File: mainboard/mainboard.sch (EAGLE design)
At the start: 1 part, among them IC1 ATMEGA168-PU

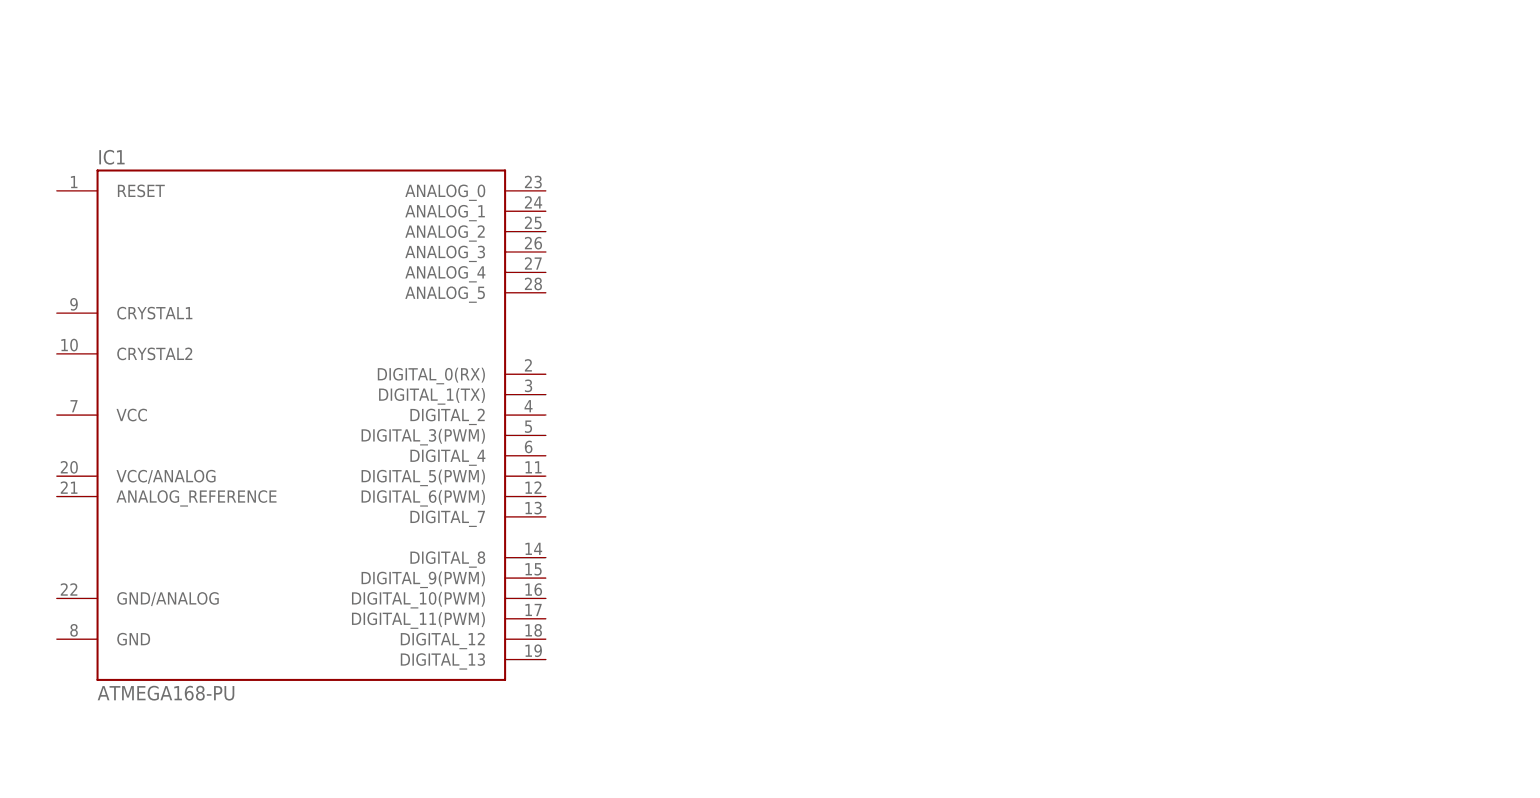
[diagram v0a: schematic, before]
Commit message: complete arduino usb with usb & programming header
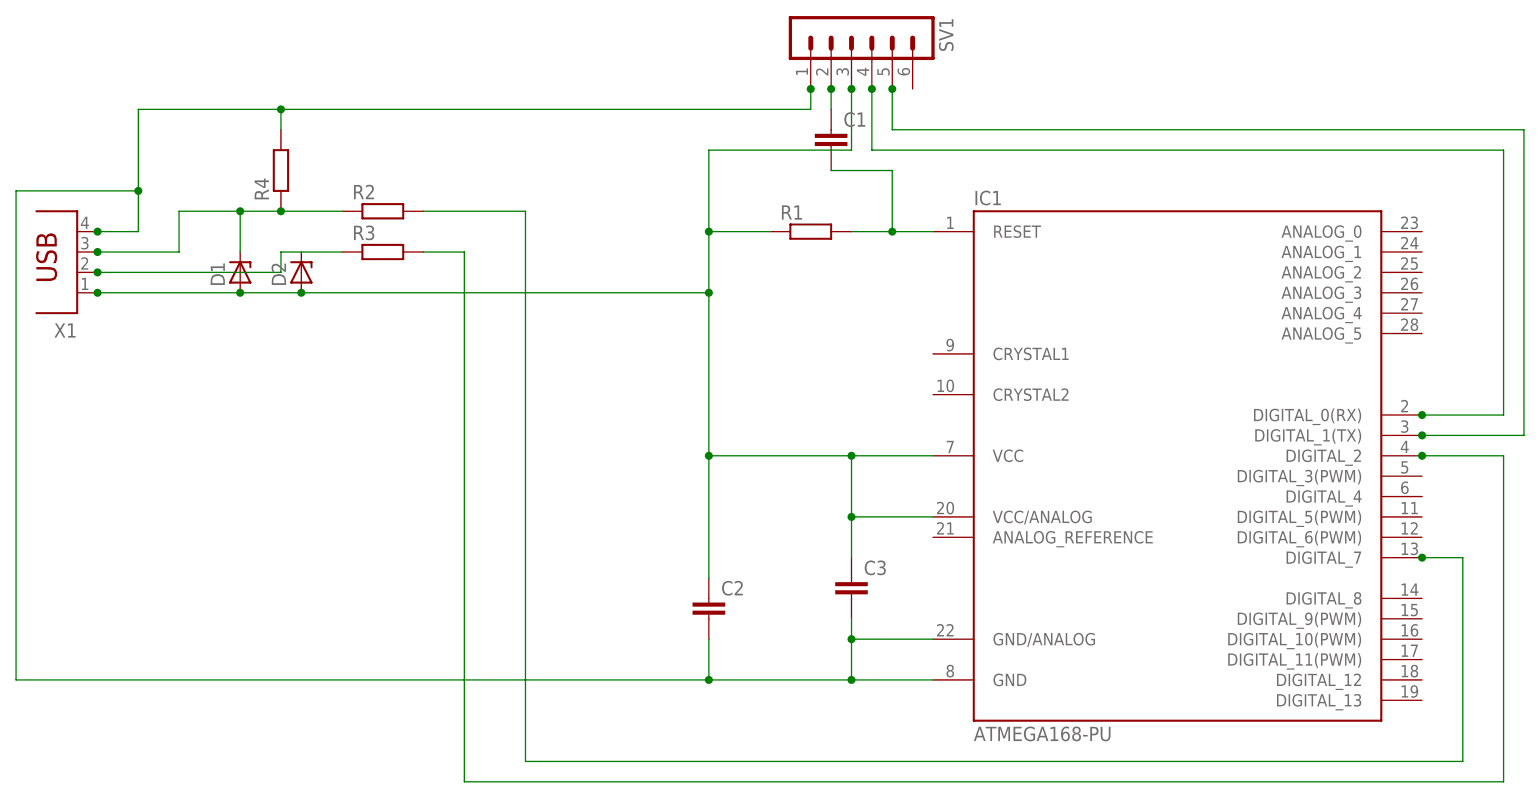
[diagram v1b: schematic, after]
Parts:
- added C1, C2, C3: (no value), capacitor-wima:C2,5-3
- added D1, D2: (no value), diode:ZENER-DIODEZD-5
- added R1, R2, R3, R4: (no value), resistor:R-EU_0204/7
- added SV1: (no value), con-lstb:MA06-1
- added X1: (no value), con-berg:PN61729
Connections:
- new net N$1: C1.2, IC1.RESET, R1.2
- new net N$10: IC1.DIGITAL_2, R3.2
- new net N$11: IC1.DIGITAL_7, R2.2
- new net N$2: D1.C, R2.1, R4.1, X1.3
- new net N$4: C1.1, SV1.2
- new net N$5: R3.1, X1.2
- new net N$6: IC1.DIGITAL_0(RX), SV1.4
- new net N$7: IC1.DIGITAL_1(TX), SV1.5
- new net N$8: C2.2, C3.2, IC1.GND, IC1.GND/ANALOG, R4.2, SV1.1, X1.4
- new net N$9: C2.1, C3.1, D1.A, D2.A, IC1.VCC, IC1.VCC/ANALOG, R1.1, SV1.3, X1.1
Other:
- moved on the sheet: IC1
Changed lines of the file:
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@@
 <parts>
 <part name="IC1" library="Arduino-AVR" deviceset="ATMEGA168-PU" device=""/>
+<part name="R1" library="resistor" deviceset="R-EU_" device="0204/7"/>
+<part name="C2" library="capacitor-wima" deviceset="C" device="2,5-3"/>
+<part name="C3" library="capacitor-wima" deviceset="C" device="2,5-3"/>
+<part name="SV1" library="con-lstb" deviceset="MA06-1" device=""/>
+<part name="C1" library="capacitor-wima" deviceset="C" device="2,5-3"/>
+<part name="X1" library="con-berg" deviceset="PN61729" device=""/>
+<part name="R2" library="resistor" deviceset="R-EU_" device="0204/7"/>
+<part name="R3" library="resistor" deviceset="R-EU_" device="0204/7"/>
+<part name="R4" library="resistor" deviceset="R-EU_" device="0204/7"/>
+<part name="D1" library="diode" deviceset="ZENER-DIODE" device="ZD-5"/>
+<part name="D2" library="diode" deviceset="ZENER-DIODE" device="ZD-5"/>
 </parts>
 <sheets>
@@
 </plain>
 <instances>
-<instance part="IC1" gate="1" x="-17.78" y="30.48"/>
+<instance part="IC1" gate="1" x="91.44" y="25.4"/>
+<instance part="R1" gate="G$1" x="45.72" y="53.34"/>
+<instance part="C2" gate="G$1" x="33.02" y="7.62"/>
+<instance part="C3" gate="G$1" x="50.8" y="10.16"/>
+<instance part="SV1" gate="1" x="53.34" y="78.74" rot="R270"/>
+<instance part="C1" gate="G$1" x="48.26" y="66.04"/>
+<instance part="X1" gate="G$1" x="-45.72" y="50.8" rot="R180"/>
+<instance part="R2" gate="G$1" x="-7.62" y="55.88"/>
+<instance part="R3" gate="G$1" x="-7.62" y="50.8"/>
+<instance part="R4" gate="G$1" x="-20.32" y="60.96" rot="R90"/>
+<instance part="D1" gate="G$1" x="-25.4" y="48.26" rot="R90"/>
+<instance part="D2" gate="G$1" x="-17.78" y="48.26" rot="R90"/>
 </instances>
 <busses>
 </busses>
 <nets>
+<net name="N$1" class="0">
+<segment>
+<pinref part="IC1" gate="1" pin="RESET"/>
+<pinref part="R1" gate="G$1" pin="2"/>
+<wire x1="50.8" y1="53.34" x2="55.88" y2="53.34" width="0.1524" layer="91"/>
+<pinref part="C1" gate="G$1" pin="2"/>
+<wire x1="55.88" y1="53.34" x2="60.96" y2="53.34" width="0.1524" layer="91"/>
+<wire x1="48.26" y1="60.96" x2="55.88" y2="60.96" width="0.1524" layer="91"/>
+<wire x1="55.88" y1="60.96" x2="55.88" y2="53.34" width="0.1524" layer="91"/>
+<junction x="55.88" y="53.34"/>
+</segment>
+</net>
+<net name="N$4" class="0">
+<segment>
+<pinref part="SV1" gate="1" pin="2"/>
+<pinref part="C1" gate="G$1" pin="1"/>
+<wire x1="48.26" y1="71.12" x2="48.26" y2="68.58" width="0.1524" layer="91"/>
+<junction x="48.26" y="71.12"/>
+</segment>
+</net>
+<net name="N$6" class="0">
+<segment>
+<pinref part="SV1" gate="1" pin="4"/>
+<wire x1="53.34" y1="71.12" x2="53.34" y2="63.5" width="0.1524" layer="91"/>
+<wire x1="53.34" y1="63.5" x2="132.08" y2="63.5" width="0.1524" layer="91"/>
+<wire x1="132.08" y1="63.5" x2="132.08" y2="30.48" width="0.1524" layer="91"/>
+<pinref part="IC1" gate="1" pin="DIGITAL_0(RX)"/>
+<wire x1="132.08" y1="30.48" x2="121.92" y2="30.48" width="0.1524" layer="91"/>
+<junction x="121.92" y="30.48"/>
+<junction x="53.34" y="71.12"/>
+</segment>
+</net>
+<net name="N$7" class="0">
+<segment>
+<pinref part="SV1" gate="1" pin="5"/>
+<wire x1="55.88" y1="71.12" x2="55.88" y2="66.04" width="0.1524" layer="91"/>
+<wire x1="55.88" y1="66.04" x2="134.62" y2="66.04" width="0.1524" layer="91"/>
+<wire x1="134.62" y1="66.04" x2="134.62" y2="27.94" width="0.1524" layer="91"/>
+<pinref part="IC1" gate="1" pin="DIGITAL_1(TX)"/>
+<wire x1="134.62" y1="27.94" x2="121.92" y2="27.94" width="0.1524" layer="91"/>
+<junction x="121.92" y="27.94"/>
+<junction x="55.88" y="71.12"/>
+</segment>
+</net>
+<net name="N$8" class="0">
+<segment>
+<pinref part="SV1" gate="1" pin="1"/>
+<junction x="45.72" y="71.12"/>
+<wire x1="45.72" y1="68.58" x2="45.72" y2="71.12" width="0.1524" layer="91"/>
+<wire x1="-38.1" y1="68.58" x2="-20.32" y2="68.58" width="0.1524" layer="91"/>
+<pinref part="IC1" gate="1" pin="GND"/>
+<pinref part="C2" gate="G$1" pin="2"/>
+<wire x1="-20.32" y1="68.58" x2="45.72" y2="68.58" width="0.1524" layer="91"/>
+<wire x1="60.96" y1="-2.54" x2="50.8" y2="-2.54" width="0.1524" layer="91"/>
+<wire x1="50.8" y1="-2.54" x2="33.02" y2="-2.54" width="0.1524" layer="91"/>
+<wire x1="33.02" y1="-2.54" x2="33.02" y2="2.54" width="0.1524" layer="91"/>
+<junction x="50.8" y="-2.54"/>
+<junction x="33.02" y="-2.54"/>
+<pinref part="IC1" gate="1" pin="GND/ANALOG"/>
+<wire x1="60.96" y1="2.54" x2="50.8" y2="2.54" width="0.1524" layer="91"/>
+<pinref part="C3" gate="G$1" pin="2"/>
+<wire x1="50.8" y1="2.54" x2="50.8" y2="5.08" width="0.1524" layer="91"/>
+<wire x1="50.8" y1="-2.54" x2="50.8" y2="2.54" width="0.1524" layer="91"/>
+<junction x="50.8" y="2.54"/>
+<wire x1="33.02" y1="-2.54" x2="-53.34" y2="-2.54" width="0.1524" layer="91"/>
+<wire x1="-53.34" y1="-2.54" x2="-53.34" y2="58.42" width="0.1524" layer="91"/>
+<wire x1="-53.34" y1="58.42" x2="-38.1" y2="58.42" width="0.1524" layer="91"/>
+<wire x1="-38.1" y1="58.42" x2="-38.1" y2="53.34" width="0.1524" layer="91"/>
+<pinref part="X1" gate="G$1" pin="4"/>
+<wire x1="-38.1" y1="53.34" x2="-43.18" y2="53.34" width="0.1524" layer="91"/>
+<wire x1="-38.1" y1="68.58" x2="-38.1" y2="58.42" width="0.1524" layer="91"/>
+<pinref part="R4" gate="G$1" pin="2"/>
+<wire x1="-20.32" y1="66.04" x2="-20.32" y2="68.58" width="0.1524" layer="91"/>
+<junction x="-20.32" y="68.58"/>
+<junction x="-43.18" y="53.34"/>
+<junction x="-38.1" y="58.42"/>
+</segment>
+</net>
+<net name="N$9" class="0">
+<segment>
+<pinref part="SV1" gate="1" pin="3"/>
+<junction x="50.8" y="71.12"/>
+<wire x1="50.8" y1="63.5" x2="50.8" y2="71.12" width="0.1524" layer="91"/>
+<wire x1="50.8" y1="63.5" x2="33.02" y2="63.5" width="0.1524" layer="91"/>
+<pinref part="IC1" gate="1" pin="VCC/ANALOG"/>
+<wire x1="60.96" y1="17.78" x2="50.8" y2="17.78" width="0.1524" layer="91"/>
+<pinref part="C3" gate="G$1" pin="1"/>
+<wire x1="50.8" y1="17.78" x2="50.8" y2="12.7" width="0.1524" layer="91"/>
+<pinref part="C2" gate="G$1" pin="1"/>
+<wire x1="33.02" y1="10.16" x2="33.02" y2="25.4" width="0.1524" layer="91"/>
+<wire x1="33.02" y1="25.4" x2="33.02" y2="45.72" width="0.1524" layer="91"/>
+<pinref part="R1" gate="G$1" pin="1"/>
+<wire x1="33.02" y1="45.72" x2="33.02" y2="53.34" width="0.1524" layer="91"/>
+<wire x1="40.64" y1="53.34" x2="33.02" y2="53.34" width="0.1524" layer="91"/>
+<pinref part="IC1" gate="1" pin="VCC"/>
+<wire x1="60.96" y1="25.4" x2="50.8" y2="25.4" width="0.1524" layer="91"/>
+<junction x="33.02" y="25.4"/>
+<wire x1="50.8" y1="25.4" x2="33.02" y2="25.4" width="0.1524" layer="91"/>
+<wire x1="50.8" y1="17.78" x2="50.8" y2="25.4" width="0.1524" layer="91"/>
+<junction x="50.8" y="25.4"/>
+<junction x="50.8" y="17.78"/>
+<wire x1="33.02" y1="63.5" x2="33.02" y2="53.34" width="0.1524" layer="91"/>
+<pinref part="X1" gate="G$1" pin="1"/>
+<wire x1="-43.18" y1="45.72" x2="-25.4" y2="45.72" width="0.1524" layer="91"/>
+<pinref part="D1" gate="G$1" pin="A"/>
+<wire x1="-25.4" y1="45.72" x2="-17.78" y2="45.72" width="0.1524" layer="91"/>
+<junction x="-25.4" y="45.72"/>
+<pinref part="D2" gate="G$1" pin="A"/>
+<wire x1="-17.78" y1="45.72" x2="33.02" y2="45.72" width="0.1524" layer="91"/>
+<junction x="-17.78" y="45.72"/>
+<junction x="-43.18" y="45.72"/>
+<junction x="33.02" y="45.72"/>
+<junction x="33.02" y="53.34"/>
+</segment>
+</net>
+<net name="N$2" class="0">
+<segment>
+<pinref part="X1" gate="G$1" pin="3"/>
+<wire x1="-43.18" y1="50.8" x2="-33.02" y2="50.8" width="0.1524" layer="91"/>
+<wire x1="-33.02" y1="50.8" x2="-33.02" y2="55.88" width="0.1524" layer="91"/>
+<pinref part="R2" gate="G$1" pin="1"/>
+<wire x1="-33.02" y1="55.88" x2="-25.4" y2="55.88" width="0.1524" layer="91"/>
+<pinref part="D1" gate="G$1" pin="C"/>
+<wire x1="-25.4" y1="55.88" x2="-20.32" y2="55.88" width="0.1524" layer="91"/>
+<wire x1="-20.32" y1="55.88" x2="-12.7" y2="55.88" width="0.1524" layer="91"/>
+<wire x1="-25.4" y1="50.8" x2="-25.4" y2="55.88" width="0.1524" layer="91"/>
+<pinref part="R4" gate="G$1" pin="1"/>
+<junction x="-20.32" y="55.88"/>
+<junction x="-25.4" y="55.88"/>
+<junction x="-43.18" y="50.8"/>
+</segment>
+</net>
+<net name="N$5" class="0">
+<segment>
+<pinref part="X1" gate="G$1" pin="2"/>
+<wire x1="-43.18" y1="48.26" x2="-20.32" y2="48.26" width="0.1524" layer="91"/>
+<wire x1="-20.32" y1="48.26" x2="-20.32" y2="50.8" width="0.1524" layer="91"/>
+<pinref part="R3" gate="G$1" pin="1"/>
+<wire x1="-20.32" y1="50.8" x2="-12.7" y2="50.8" width="0.1524" layer="91"/>
+<junction x="-43.18" y="48.26"/>
+</segment>
+</net>
+<net name="N$10" class="0">
+<segment>
+<pinref part="R3" gate="G$1" pin="2"/>
+<wire x1="-2.54" y1="50.8" x2="2.54" y2="50.8" width="0.1524" layer="91"/>
+<wire x1="2.54" y1="50.8" x2="2.54" y2="-15.24" width="0.1524" layer="91"/>
+<wire x1="2.54" y1="-15.24" x2="132.08" y2="-15.24" width="0.1524" layer="91"/>
+<wire x1="132.08" y1="-15.24" x2="132.08" y2="25.4" width="0.1524" layer="91"/>
+<pinref part="IC1" gate="1" pin="DIGITAL_2"/>
+<wire x1="132.08" y1="25.4" x2="121.92" y2="25.4" width="0.1524" layer="91"/>
+<junction x="121.92" y="25.4"/>
+</segment>
+</net>
+<net name="N$11" class="0">
+<segment>
+<pinref part="R2" gate="G$1" pin="2"/>
+<wire x1="-2.54" y1="55.88" x2="10.16" y2="55.88" width="0.1524" layer="91"/>
+<wire x1="10.16" y1="55.88" x2="10.16" y2="-12.7" width="0.1524" layer="91"/>
+<wire x1="10.16" y1="-12.7" x2="127" y2="-12.7" width="0.1524" layer="91"/>
+<wire x1="127" y1="-12.7" x2="127" y2="12.7" width="0.1524" layer="91"/>
+<pinref part="IC1" gate="1" pin="DIGITAL_7"/>
+<wire x1="127" y1="12.7" x2="121.92" y2="12.7" width="0.1524" layer="91"/>
+<junction x="121.92" y="12.7"/>
+</segment>
+</net>
 </nets>
 </sheet>
 </sheets>
+<errors>
+</errors>
 </schematic>
 </drawing>

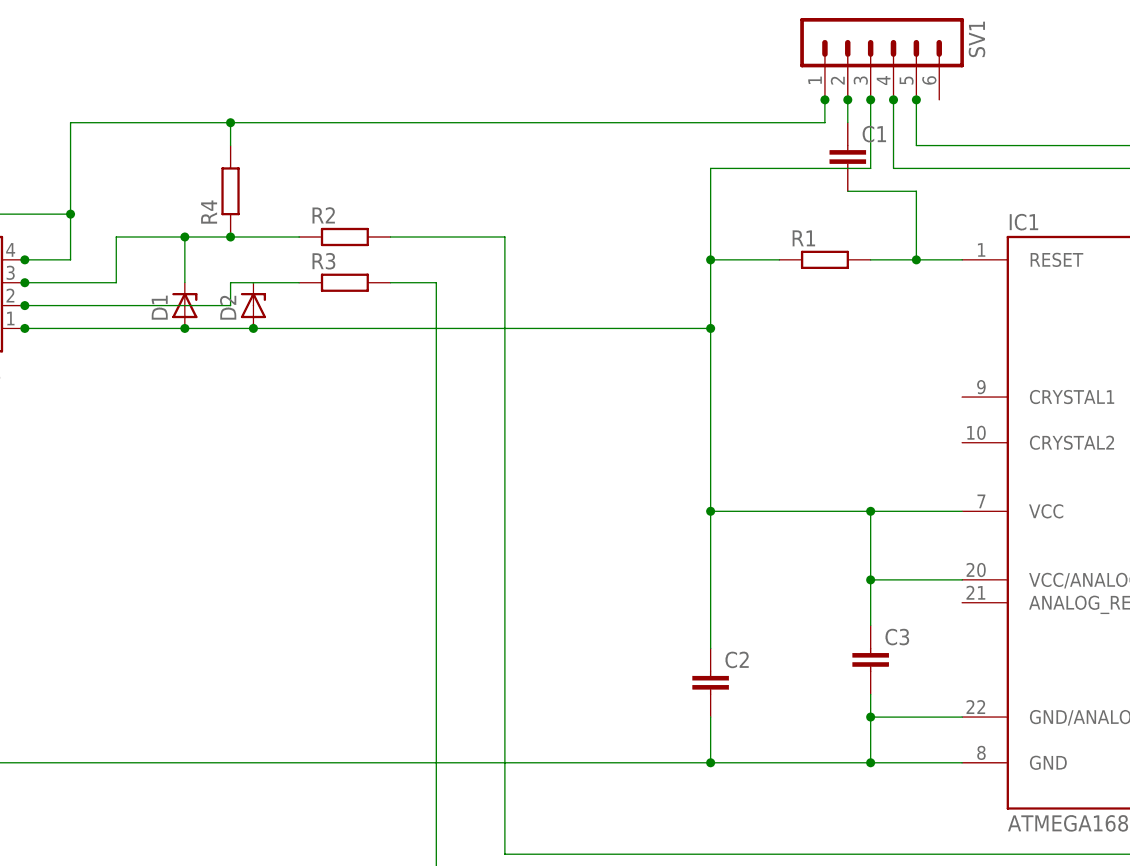
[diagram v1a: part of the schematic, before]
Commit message: printed values on parts
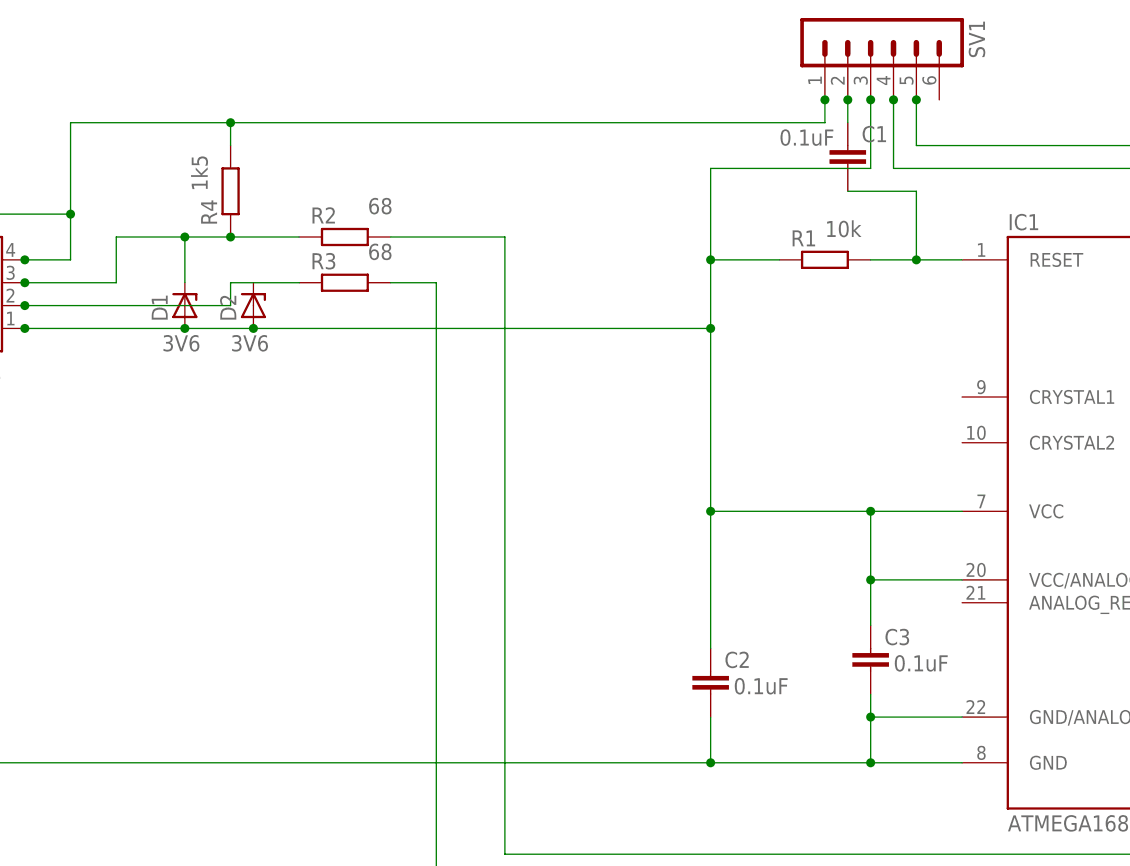
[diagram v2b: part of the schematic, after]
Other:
- note added: "0.1uF"
- note added: "10k"
- note added: "1k5"
- note added: "3V6"
- note added: "68"
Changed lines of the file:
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@@
 <sheet>
 <plain>
+<text x="-5.08" y="58.42" size="1.778" layer="96">68</text>
+<text x="-5.08" y="53.34" size="1.778" layer="96">68</text>
+<text x="-22.86" y="60.96" size="1.778" layer="96" rot="R90">1k5</text>
+<text x="45.72" y="55.88" size="1.778" layer="96">10k</text>
+<text x="35.56" y="5.08" size="1.778" layer="96">0.1uF</text>
+<text x="53.34" y="7.62" size="1.778" layer="96">0.1uF</text>
+<text x="40.64" y="66.04" size="1.778" layer="96">0.1uF</text>
+<text x="-27.94" y="43.18" size="1.778" layer="96">3V6</text>
+<text x="-20.32" y="43.18" size="1.778" layer="96">3V6</text>
 </plain>
 <instances>
